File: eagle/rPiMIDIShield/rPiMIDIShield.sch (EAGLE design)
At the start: 9 parts

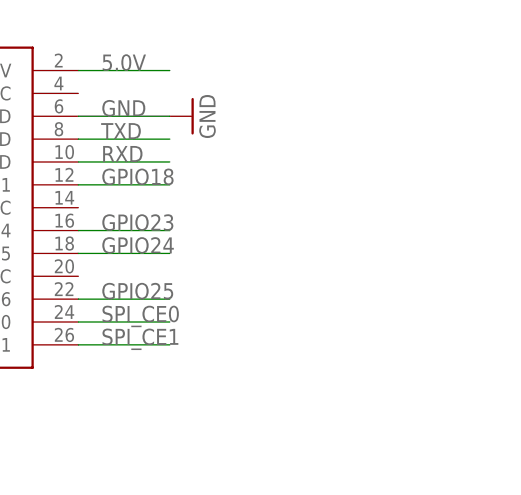
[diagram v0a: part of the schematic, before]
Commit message: Added GPIO headers to the rPI board
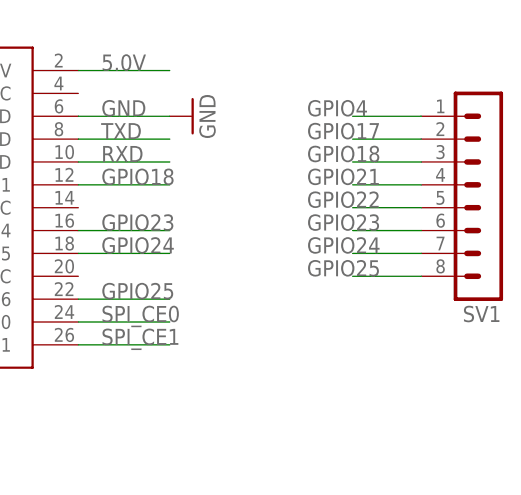
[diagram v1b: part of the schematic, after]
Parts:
- added SV1: (no value), con-lstb:MA08-1
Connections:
- net GPIO17: now also SV1.2
- net GPIO18: now also SV1.3
- net GPIO21: now also SV1.4
- net GPIO22: now also SV1.5
- net GPIO23: now also SV1.6
- net GPIO24: now also SV1.7
- net GPIO25: now also SV1.8
- net GPIO4: now also SV1.1
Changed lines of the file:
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@@
 <part name="GND2" library="supply1" deviceset="GND" device=""/>
 <part name="GND3" library="supply1" deviceset="GND" device=""/>
+<part name="SV1" library="con-lstb" deviceset="MA08-1" device=""/>
 </parts>
 <sheets>
@@
 <instance part="GND2" gate="1" x="185.42" y="58.42" rot="R90"/>
 <instance part="GND3" gate="1" x="2.54" y="45.72"/>
+<instance part="SV1" gate="1" x="218.44" y="50.8" rot="R180"/>
 </instances>
 <busses>
@@
 <label x="121.92" y="50.8" size="1.778" layer="95"/>
 <pinref part="U$1" gate="G$1" pin="GPIO0"/>
+<label x="198.12" y="55.88" size="1.778" layer="95"/>
+</segment>
+<segment>
+<wire x1="210.82" y1="55.88" x2="203.2" y2="55.88" width="0.1524" layer="91"/>
+<pinref part="SV1" gate="1" pin="2"/>
 </segment>
 </net>
@@
 <label x="175.26" y="50.8" size="1.778" layer="95"/>
 <pinref part="U$1" gate="G$1" pin="GPIO1"/>
+<label x="198.12" y="53.34" size="1.778" layer="95"/>
+</segment>
+<segment>
+<wire x1="210.82" y1="53.34" x2="203.2" y2="53.34" width="0.1524" layer="91"/>
+<pinref part="SV1" gate="1" pin="3"/>
 </segment>
 </net>
@@
 <label x="121.92" y="48.26" size="1.778" layer="95"/>
 <pinref part="U$1" gate="G$1" pin="GPIO2"/>
+<label x="198.12" y="50.8" size="1.778" layer="95"/>
+</segment>
+<segment>
+<wire x1="210.82" y1="50.8" x2="203.2" y2="50.8" width="0.1524" layer="91"/>
+<pinref part="SV1" gate="1" pin="4"/>
 </segment>
 </net>
@@
 <label x="121.92" y="45.72" size="1.778" layer="95"/>
 <pinref part="U$1" gate="G$1" pin="GPIO3"/>
+<label x="198.12" y="48.26" size="1.778" layer="95"/>
+</segment>
+<segment>
+<wire x1="210.82" y1="48.26" x2="203.2" y2="48.26" width="0.1524" layer="91"/>
+<pinref part="SV1" gate="1" pin="5"/>
 </segment>
 </net>
@@
 <label x="175.26" y="45.72" size="1.778" layer="95"/>
 <pinref part="U$1" gate="G$1" pin="GPIO4"/>
+<label x="198.12" y="45.72" size="1.778" layer="95"/>
+</segment>
+<segment>
+<wire x1="210.82" y1="45.72" x2="203.2" y2="45.72" width="0.1524" layer="91"/>
+<pinref part="SV1" gate="1" pin="6"/>
 </segment>
 </net>
@@
 <label x="175.26" y="43.18" size="1.778" layer="95"/>
 <pinref part="U$1" gate="G$1" pin="GPIO5"/>
+<label x="198.12" y="43.18" size="1.778" layer="95"/>
+</segment>
+<segment>
+<wire x1="210.82" y1="43.18" x2="203.2" y2="43.18" width="0.1524" layer="91"/>
+<pinref part="SV1" gate="1" pin="7"/>
 </segment>
 </net>
@@
 <label x="175.26" y="38.1" size="1.778" layer="95"/>
 <pinref part="U$1" gate="G$1" pin="GPIO6"/>
+<label x="198.12" y="40.64" size="1.778" layer="95"/>
+</segment>
+<segment>
+<wire x1="210.82" y1="40.64" x2="203.2" y2="40.64" width="0.1524" layer="91"/>
+<pinref part="SV1" gate="1" pin="8"/>
 </segment>
 </net>
@@
 <label x="121.92" y="55.88" size="1.778" layer="95"/>
 <pinref part="U$1" gate="G$1" pin="GPIO7"/>
+<label x="198.12" y="58.42" size="1.778" layer="95"/>
+</segment>
+<segment>
+<pinref part="SV1" gate="1" pin="1"/>
+<wire x1="210.82" y1="58.42" x2="203.2" y2="58.42" width="0.1524" layer="91"/>
 </segment>
 </net>

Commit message: Modified the labels so they don't show up on silkscreen. Also moved all components within eagle's 'Approved Board Size'
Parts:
- renumbered U$1 to GPIO
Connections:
- net GND: now also MIDIIN.PE, MIDIOUT.2

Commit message: started adding switches for 5v power over MIDI
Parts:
- added SV2: (no value), con-lstb:MA03-1
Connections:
- new net N$2: SV2.2
- net 5.0V: now also SV2.1
- net GND: now also SV2.3
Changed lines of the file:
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@@
 <part name="GND4" library="supply1" deviceset="GND" device=""/>
 <part name="GND5" library="supply1" deviceset="GND" device=""/>
+<part name="SV2" library="con-lstb" deviceset="MA03-1" device=""/>
+<part name="GND6" library="supply1" deviceset="GND" device=""/>
 </parts>
 <sheets>
@@
 <instance part="GND4" gate="1" x="10.16" y="45.72"/>
 <instance part="GND5" gate="1" x="10.16" y="15.24"/>
+<instance part="SV2" gate="G$1" x="78.74" y="66.04" rot="R180"/>
+<instance part="GND6" gate="1" x="66.04" y="60.96"/>
 </instances>
 <busses>
@@
 <pinref part="GPIO" gate="G$1" pin="5.0V@1"/>
 <label x="53.34" y="53.34" size="1.778" layer="95"/>
+<label x="66.04" y="68.58" size="1.778" layer="95"/>
 </segment>
 <segment>
 <pinref part="R3" gate="G$1" pin="2"/>
 <wire x1="53.34" y1="53.34" x2="60.96" y2="53.34" width="0.1524" layer="91"/>
+</segment>
+<segment>
+<pinref part="SV2" gate="G$1" pin="1"/>
+<wire x1="66.04" y1="68.58" x2="71.12" y2="68.58" width="0.1524" layer="91"/>
 </segment>
 </net>
@@
 <pinref part="MIDIIN" gate="G$1" pin="PE"/>
 <pinref part="GND5" gate="1" pin="GND"/>
+</segment>
+<segment>
+<pinref part="SV2" gate="G$1" pin="3"/>
+<wire x1="71.12" y1="63.5" x2="66.04" y2="63.5" width="0.1524" layer="91"/>
+<pinref part="GND6" gate="1" pin="GND"/>
 </segment>
 </net>
@@
 </segment>
 </net>
+<net name="N$2" class="0">
+<segment>
+<pinref part="SV2" gate="G$1" pin="2"/>
+<wire x1="66.04" y1="66.04" x2="71.12" y2="66.04" width="0.1524" layer="91"/>
+</segment>
+</net>

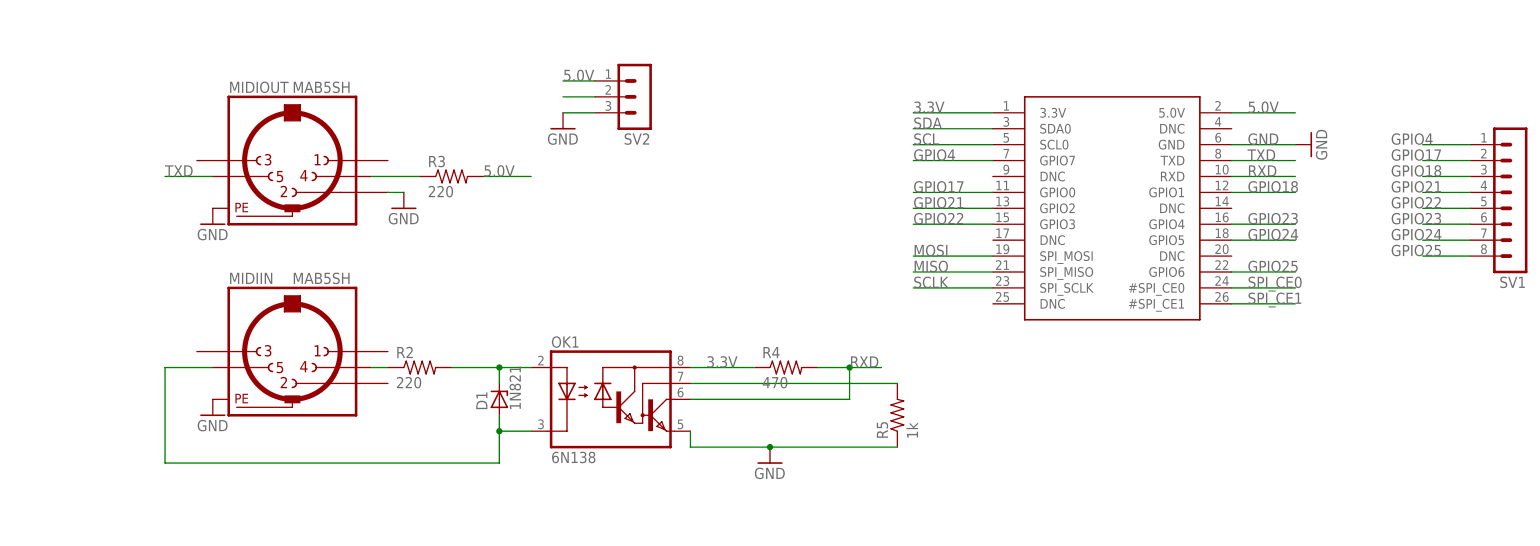
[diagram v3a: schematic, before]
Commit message: Added switches for 5v supply via MIDI
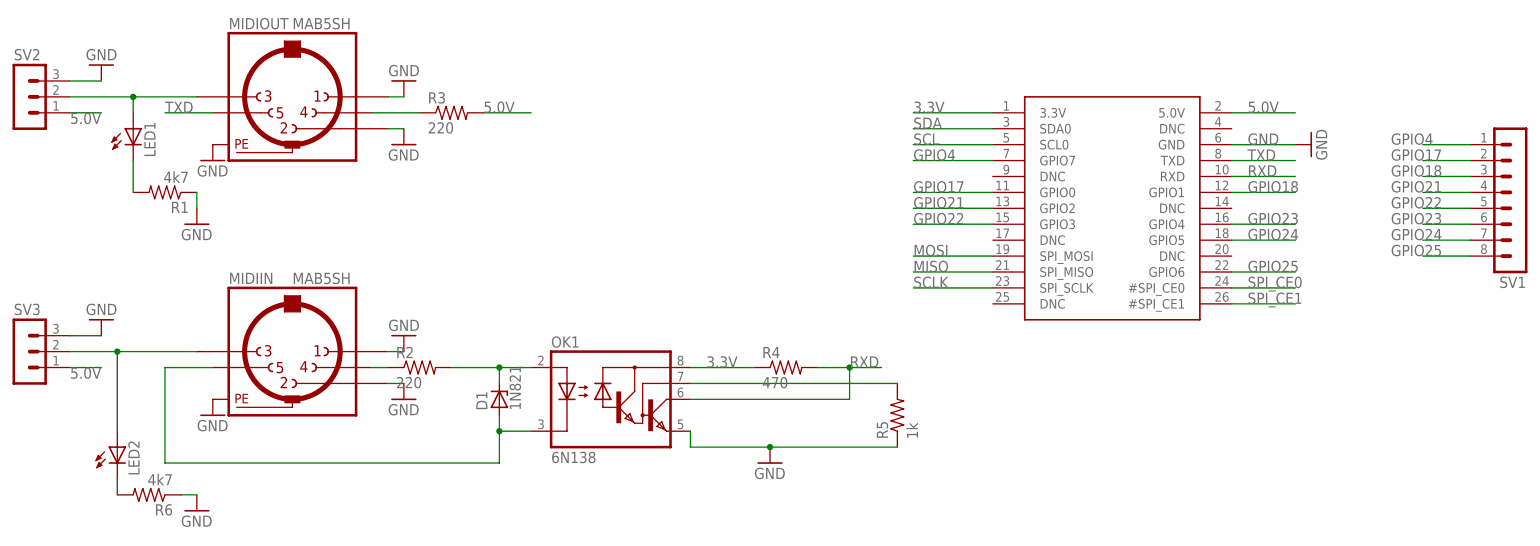
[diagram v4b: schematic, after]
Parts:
- added LED1, LED2: (no value), led:LEDLSU260
- added R1, R6: 4k7, resistor:R-US_0204/7
- added SV3: (no value), con-lstb:MA03-1
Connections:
- new net N$1: LED2.A, MIDIIN.3, SV3.2
- new net N$13: LED2.C, R6.2
- new net N$5: LED1.C, R1.2
- net 5.0V: now also SV3.1
- net GND: now also MIDIIN.1, MIDIIN.2, MIDIOUT.1, R1.1, R6.1, SV3.3
- net N$2: now also LED1.A, MIDIOUT.3
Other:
- moved on the sheet: MIDIOUT, R3, SV2
